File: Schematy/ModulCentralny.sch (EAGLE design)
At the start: 47 parts, among them X1 GLX-S-88M

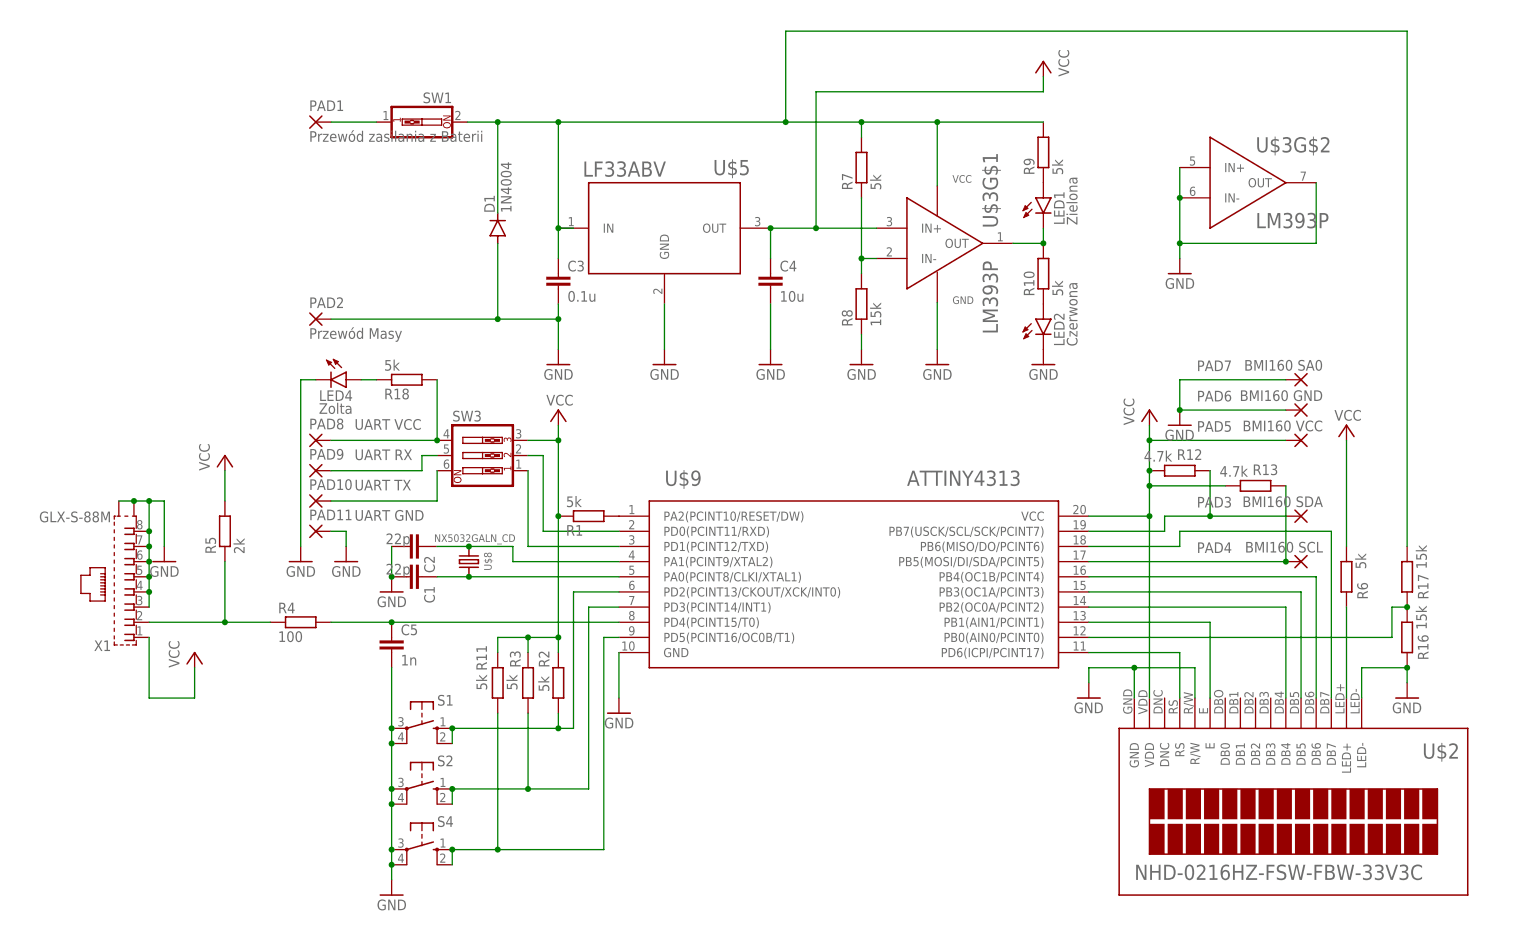
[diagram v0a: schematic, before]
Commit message: Dodanie podciągającego rezystora na wyjście lm393
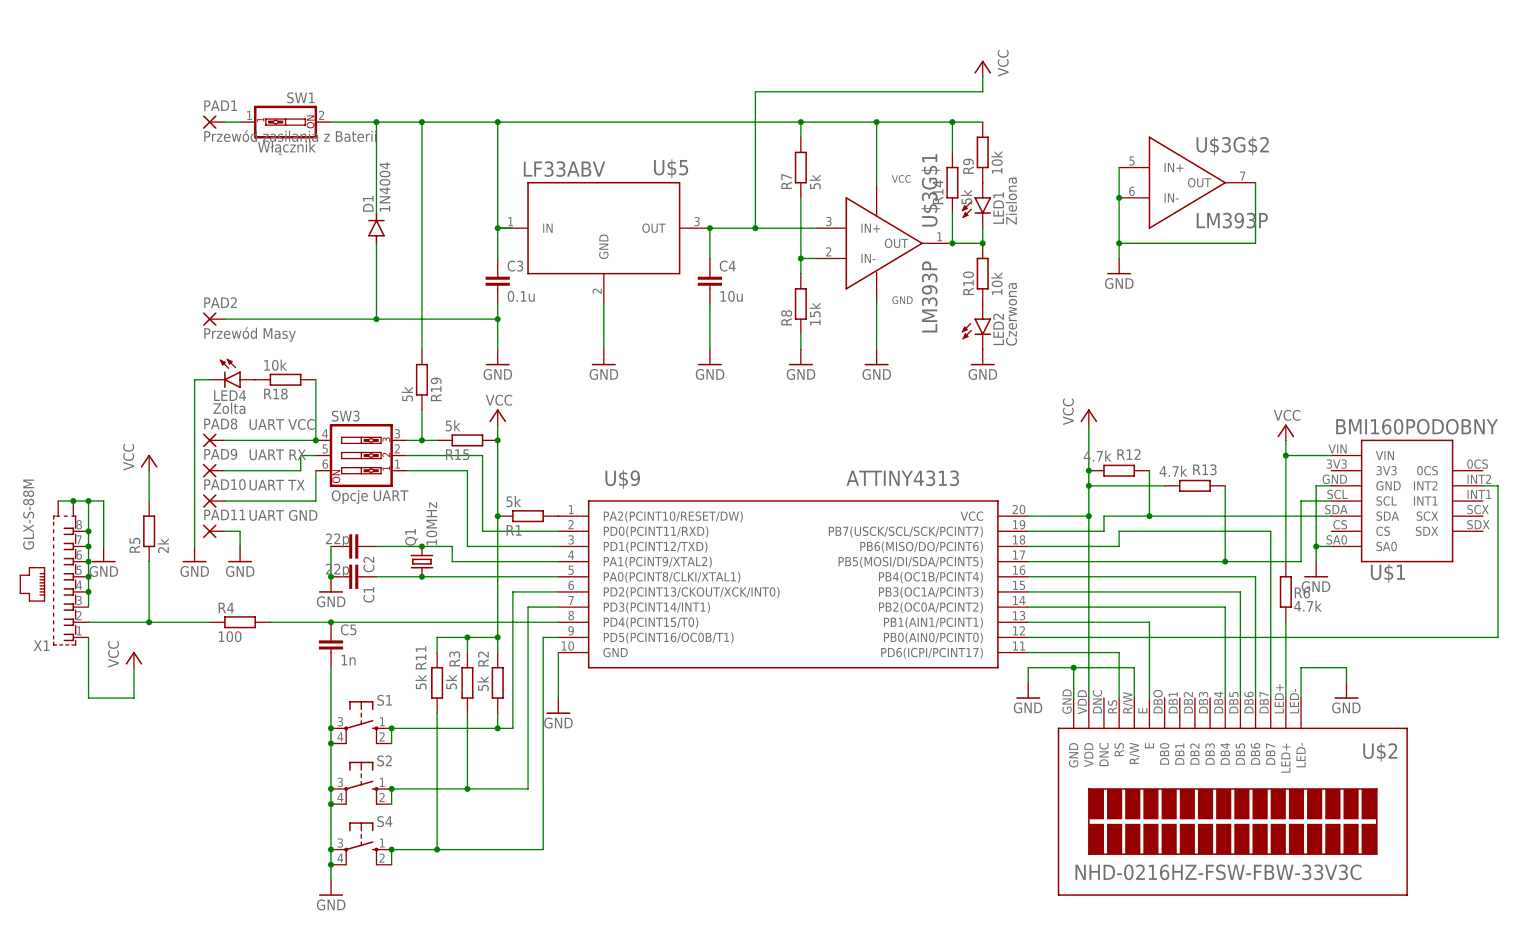
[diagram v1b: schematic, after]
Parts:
- removed PAD3: BMI160 SDA, wirepad:WIREPADSMD1,27-254
- removed PAD4: BMI160 SCL, wirepad:WIREPADSMD1,27-254
- removed PAD5: BMI160 VCC, wirepad:WIREPADSMD1,27-254
- removed PAD6: BMI160 GND, wirepad:WIREPADSMD1,27-254
- removed PAD7: BMI160 SA0, wirepad:WIREPADSMD1,27-254
- removed R16, R17: 15k, rcl:R-EU_0207/7
- removed U$8: NX5032GALN_CD, BezkonataktowyLicznikObrotów:NX5032GALN_CD
- added Q1: 10MHz, crystal:CRYSTALHC49U70
- added R14, R15, R19: 5k, rcl:R-EU_0207/7
- added U$1: BMI160PODOBNY, BezkonataktowyLicznikObrotów:BMI160PODOBNY
- PAD1, PAD2: device wirepad:WIREPADSMD1,27-254 -> wirepad:WIREPAD2,54/1,1
- R10, R18, R9: value 5k -> 10k
- R6: value 5k -> 4.7k
- SW1: value (none) -> Włącznik
- SW3: value (none) -> Opcje UART
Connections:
- removed net N$33: R16.2, R17.1, U$9.PB0(AIN0/PCINT0)
- new net N$14: R15.1, R19.1, SW3.3
- new net N$24: U$1.INT2, U$9.PB0(AIN0/PCINT0)
- net GND: now also U$1.GND, U$1.SA0; no longer PAD6.P, PAD7.P, R16.1
- net N$1: now also U$1.SCL; no longer PAD4.P
- net N$15: now also Q1.1; no longer U$8.1
- net N$16: now also R6.2; no longer R6.1
- net N$17: now also R14.2, R19.2; no longer R17.2
- net N$18: now also U$1.SDA; no longer PAD3.P
- net N$2: now also Q1.2; no longer U$8.2
- net N$20: now also R14.1
- net VCC: now also R15.2, R6.1, U$1.VIN; no longer PAD5.P, R6.2, SW3.3
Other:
- moved on the sheet: C1, C2, C3, C4, C5, D1, LED1, LED2, LED4, PAD1, PAD10, PAD11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

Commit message: Nowa płytka w wymiarach 6,6x9,9mm
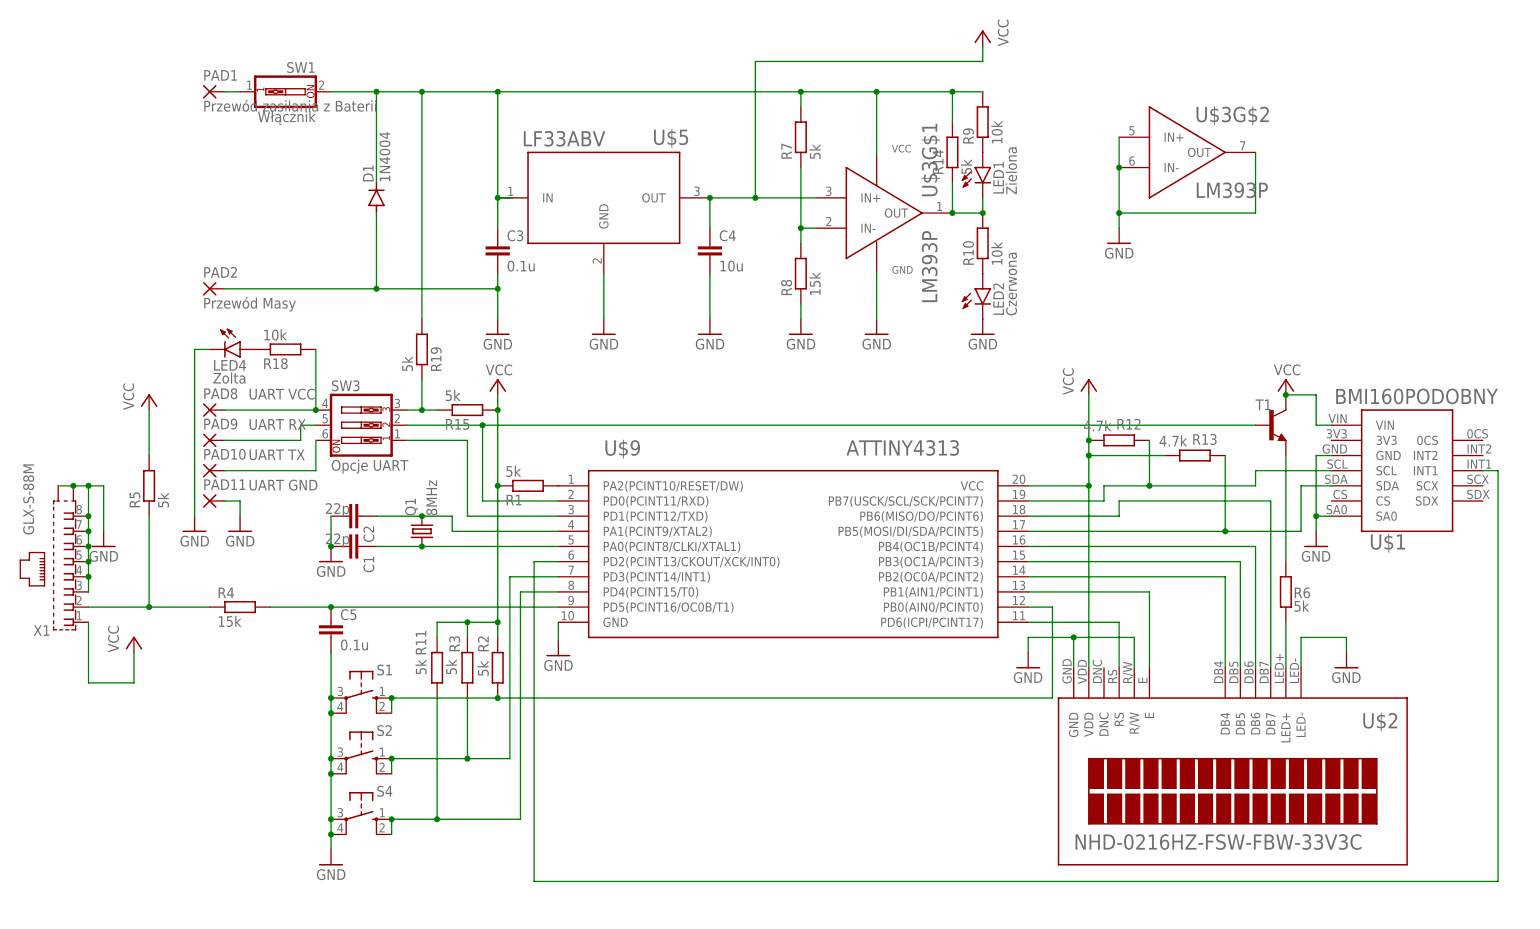
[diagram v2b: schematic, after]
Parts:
- added T1: (no value), transistor:BC547B-NPN-TO92-CBE
- C5: value 1n -> 0.1u
- Q1: value 10MHz -> 8MHz
- R4: value 100 -> 15k
- R5: value 2k -> 5k
- R6: value 4.7k -> 5k
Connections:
- new net N$25: R6.1, T1.E
- net N$1: now also U$1.SDA; no longer U$1.SCL
- net N$13: now also T1.B
- net N$18: now also U$1.SCL; no longer U$1.SDA
- net N$24: now also U$1.INT1, U$9.PD2(PCINT13/CKOUT/XCK/INT0); no longer U$1.INT2, U$9.PB0(AIN0/PCINT0)
- net N$30: now also U$9.PD5(PCINT16/OC0B/T1); no longer U$9.PD4(PCINT15/T0)
- net N$32: now also U$9.PB0(AIN0/PCINT0); no longer U$9.PD2(PCINT13/CKOUT/XCK/INT0)
- net N$4: now also U$9.PD4(PCINT15/T0); no longer U$9.PD5(PCINT16/OC0B/T1)
- net VCC: now also T1.C; no longer R6.1
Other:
- moved on the sheet: C1, C2, C3, C4, C5, D1, LED1, LED2, LED4, PAD1, PAD10, PAD11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
